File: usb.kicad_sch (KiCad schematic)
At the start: 130 parts, among them J3 USB4105-GF-A, J4 WE_632723300011_alt_symbol, U10 TUSB1046-DCI, U11 TPD4E05U06QDQARQ1, U12 AP22615, U13 TPD4E05U06QDQARQ1, U14 TPD4E05U06QDQARQ1, U15 TPD4E05U06QDQARQ1, U16 TPD4E05U06QDQARQ1, U5 FT230XQ-R, U6 TPS65988, U7 W25Q80DVUXIE_TR, U8 NCP730BMT330TBG, U9 AP22615

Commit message: Renaming Sheets
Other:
- company: Antmicro Ltd -> Dronolab
- title: Jetson Orin Baseboard -> USB Debug, DP
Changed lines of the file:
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@@
   (paper "A3")
   (title_block
-    (title "Jetson Orin Baseboard")
-    (date "2023-03-03")
-    (rev "1.1.0")
-    (company "Antmicro Ltd")
-    (comment 1 "www.antmicro.com")
+    (title "USB Debug, DP")
+    (date "2023-07-05")
+    (rev "1.0.0")
+    (company "Dronolab")
+    (comment 1 "dronolab.etsmtl.ca")
   )
   (junction (at 257.81 152.4) (diameter 0) (color 0 0 0 0)

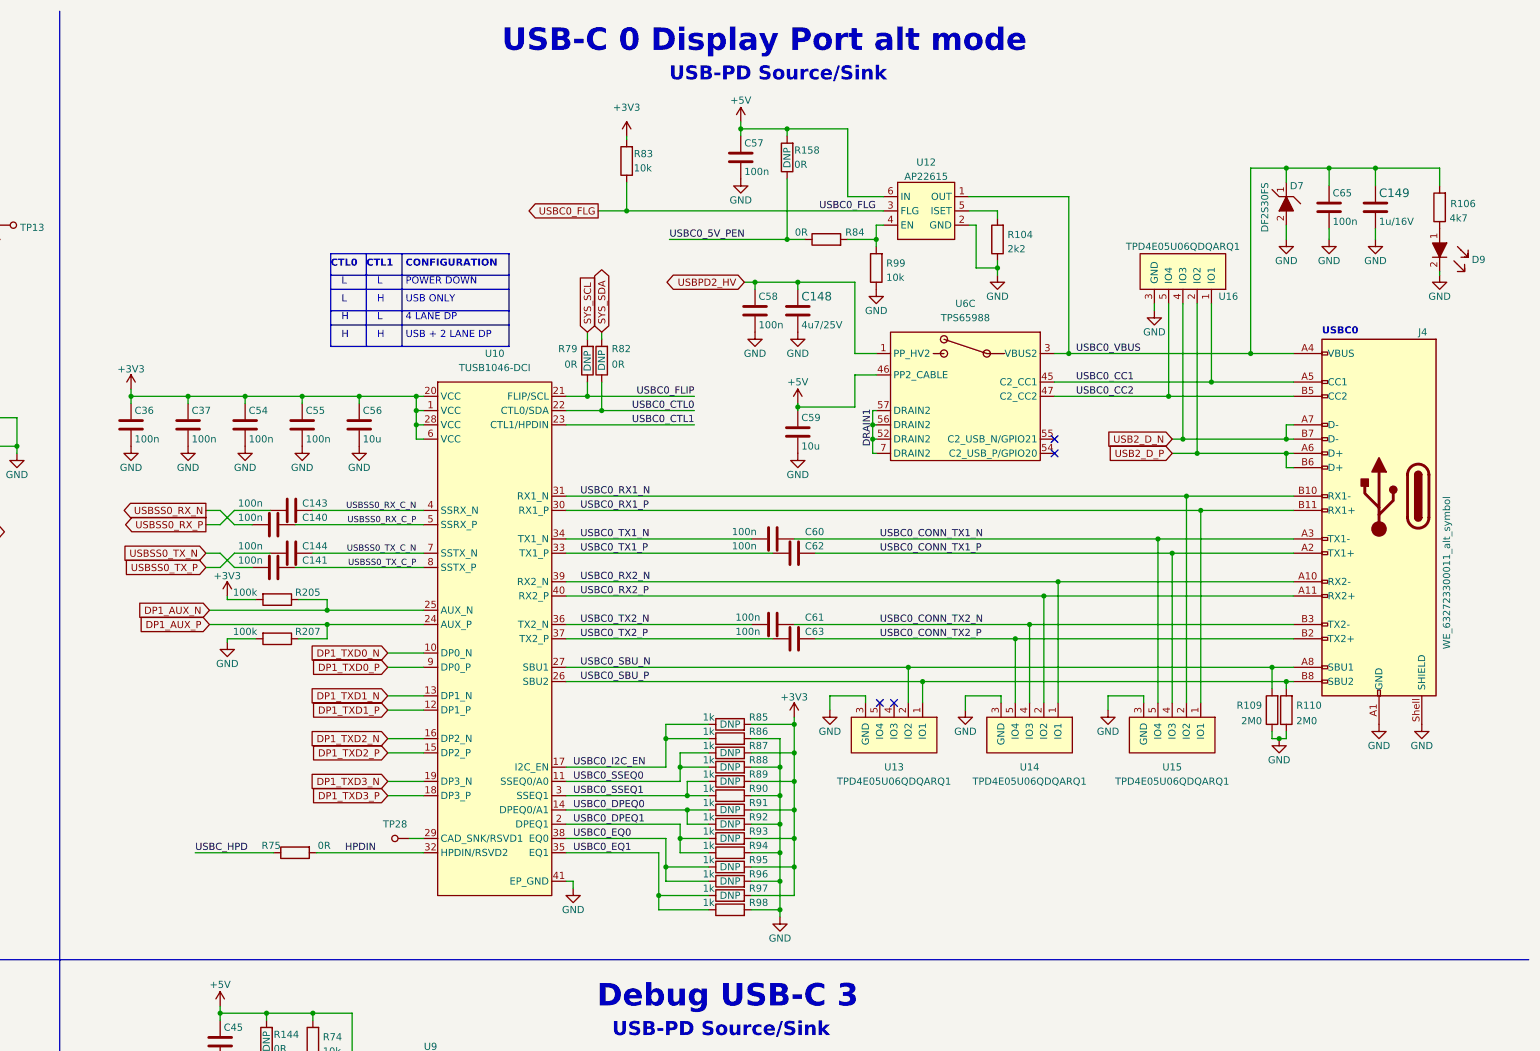
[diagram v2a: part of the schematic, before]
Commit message: Caps and DP to USBC HPD
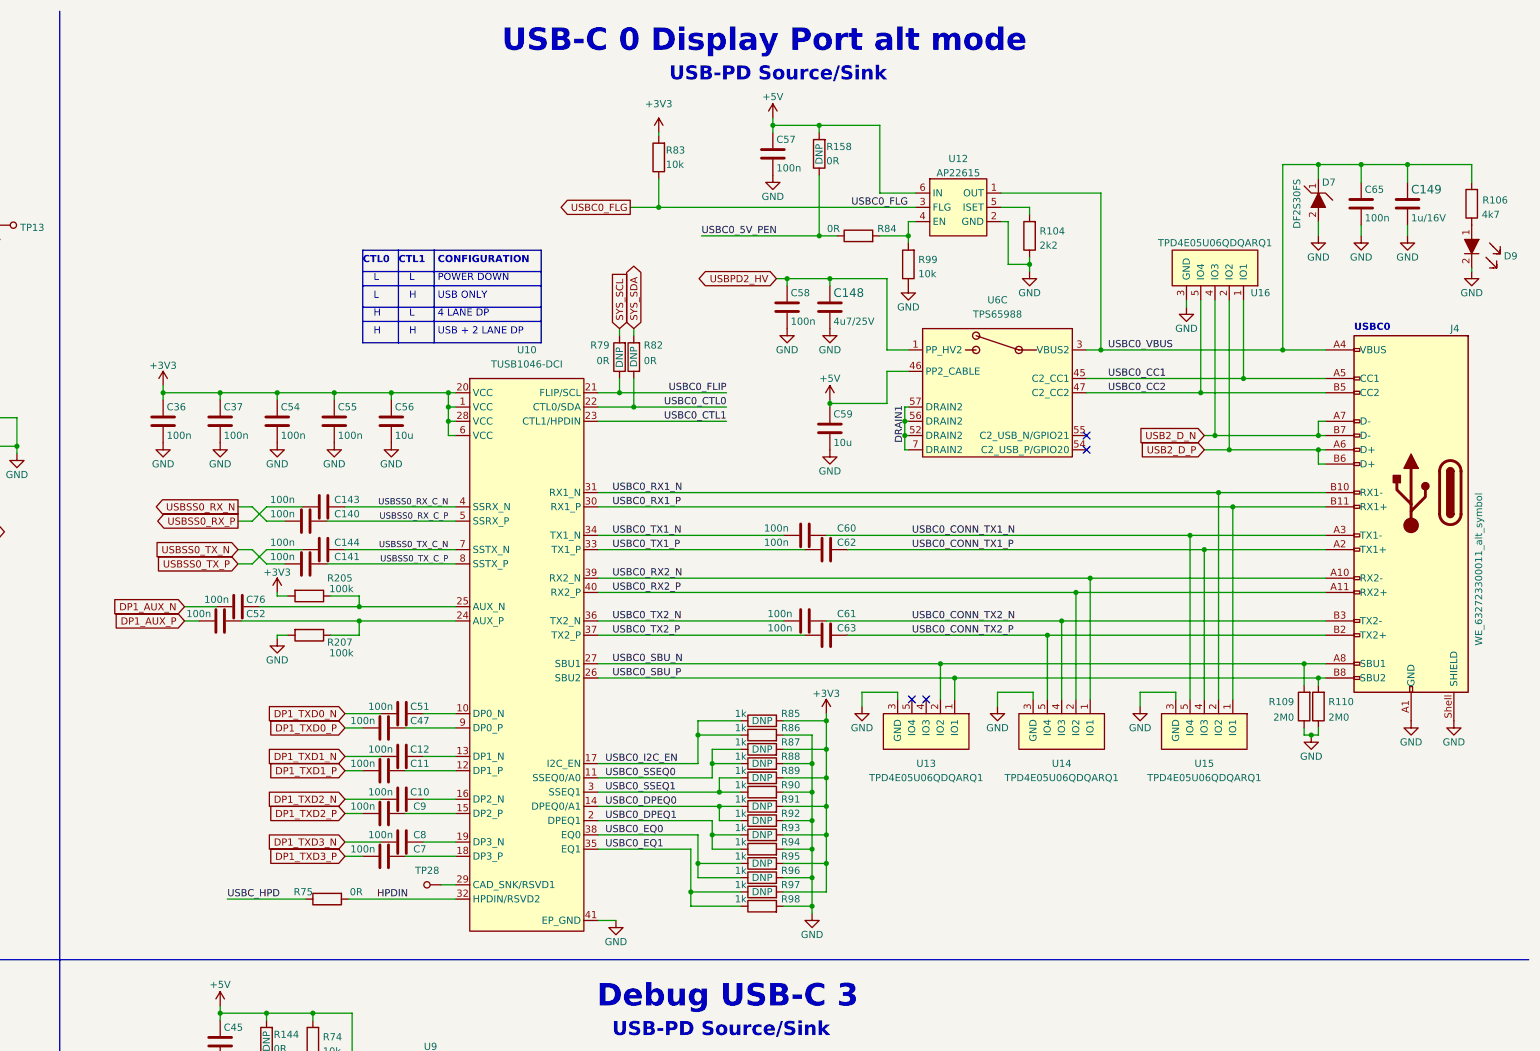
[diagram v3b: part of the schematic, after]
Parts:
- added C10, C11, C12, C47, C51, C52, C7, C76, C8, C9: 100n, symbol Device:C
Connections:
- net DP1_AUX_N: now also C76.1; no longer R205.1, U10.25 (AUX_N)
- net DP1_AUX_P: now also C52.1; no longer R207.1, U10.24 (AUX_P)
- net DP1_TXD0_N: now also C51.1; no longer U10.10 (DP0_N)
- net DP1_TXD0_P: now also C47.1; no longer U10.9 (DP0_P)
- net DP1_TXD1_N: now also C12.1; no longer U10.13 (DP1_N)
- net DP1_TXD1_P: now also C11.1; no longer U10.12 (DP1_P)
- net DP1_TXD2_N: now also C10.1; no longer U10.16 (DP2_N)
- net DP1_TXD2_P: now also C9.1; no longer U10.15 (DP2_P)
- net DP1_TXD3_N: now also C8.1; no longer U10.19 (DP3_N)
- net DP1_TXD3_P: now also C7.1; no longer U10.18 (DP3_P)
- new net: C47.2, U10.9 (DP0_P)
- new net: C76.2, R205.1, U10.25 (AUX_N)
- new net: C52.2, R207.1, U10.24 (AUX_P)
- new net: C11.2, U10.12 (DP1_P)
- new net: C7.2, U10.18 (DP3_P)
- new net: C51.2, U10.10 (DP0_N)
- new net: C12.2, U10.13 (DP1_N)
- new net: C9.2, U10.15 (DP2_P)
- new net: C10.2, U10.16 (DP2_N)
- new net: C8.2, U10.19 (DP3_N)
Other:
- moved on the sheet: C140, C141, C143, C144, C148, C149, C36, C37, C54, C55, C56, C57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

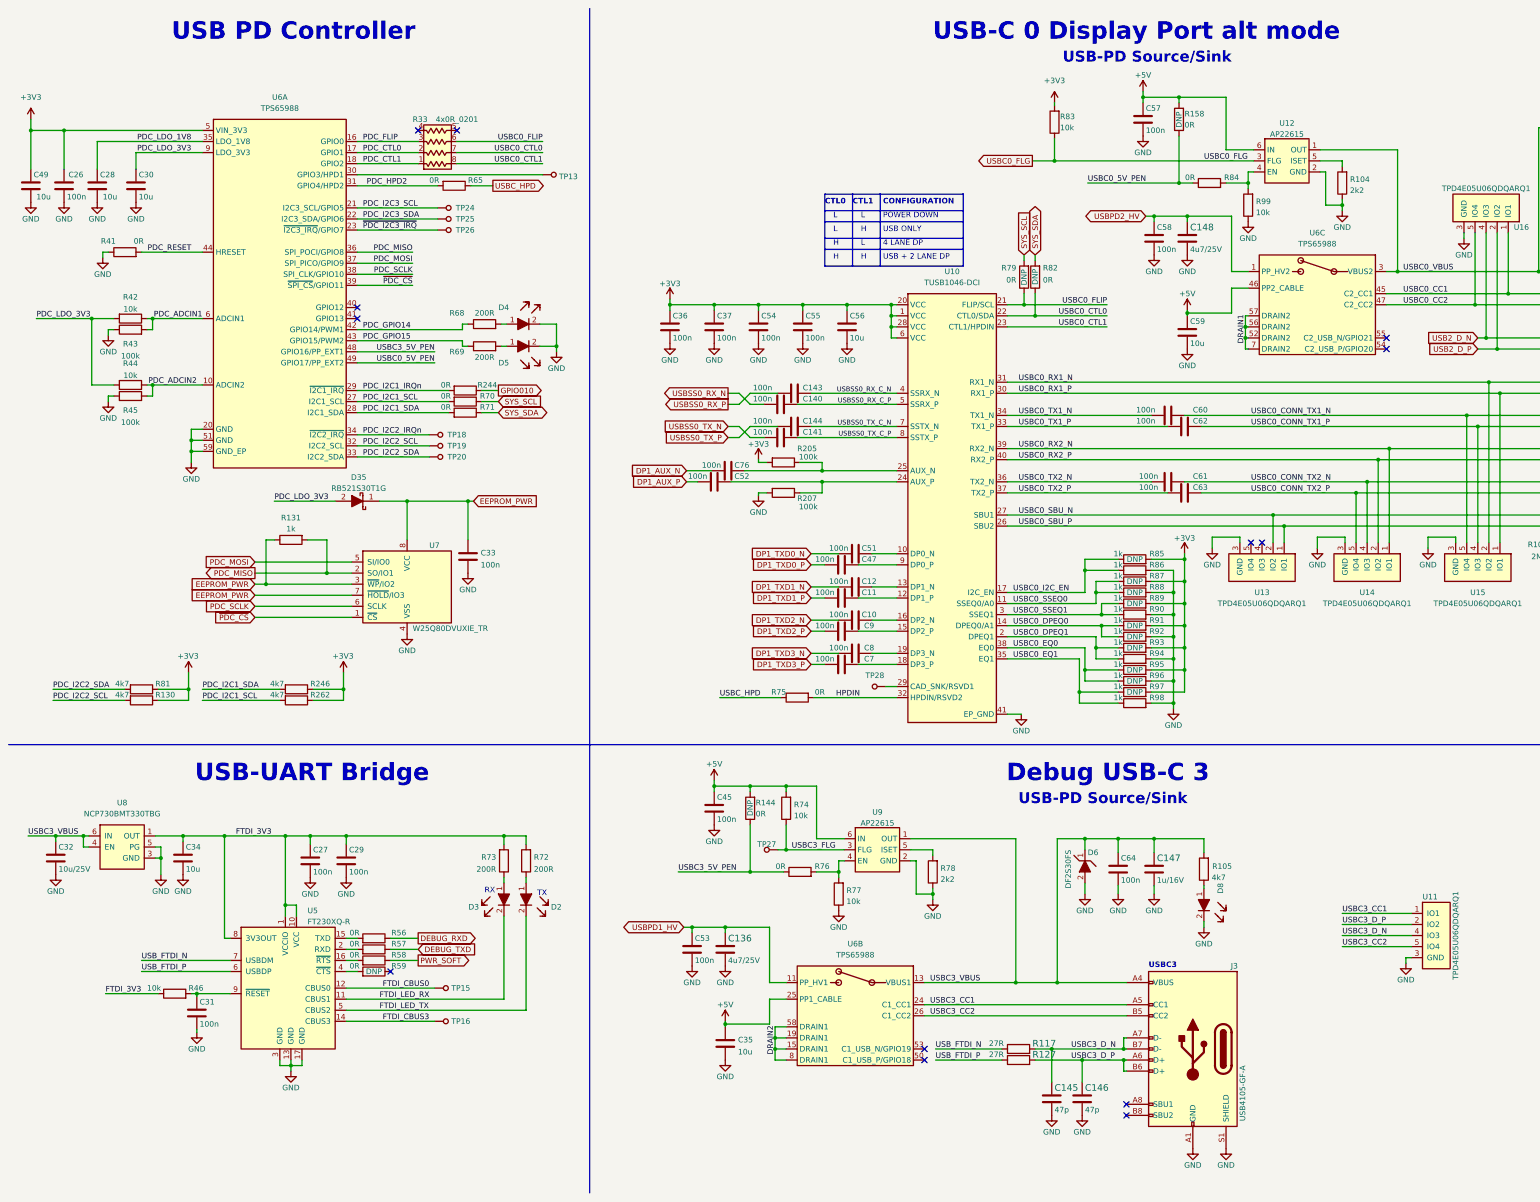
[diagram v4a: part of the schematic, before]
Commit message: Merge du usb-c debug et usb-c 1 et suppression de usb-c 3
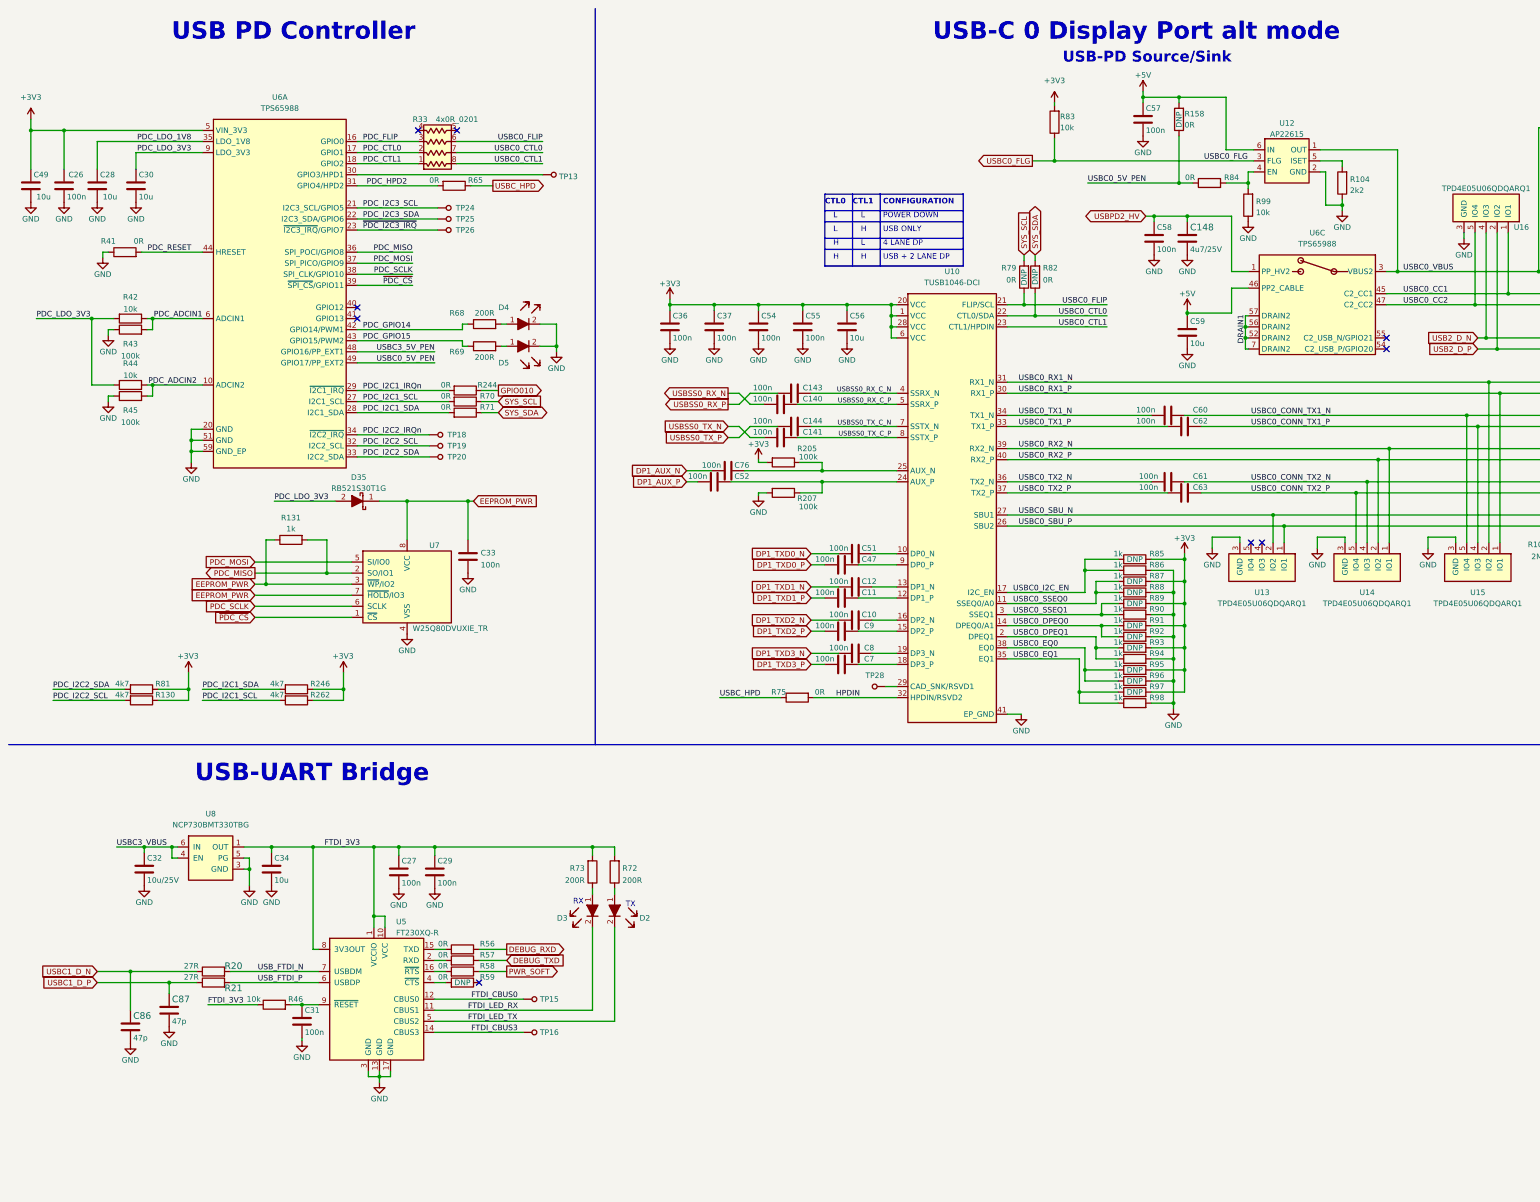
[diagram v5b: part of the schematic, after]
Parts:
- removed C136: C_4u7_0402_25V, jetson-orin-baseboard-footprints:0402-cap, symbol jetson-orin-baseboard:C_4u7_0402_25V
- removed C145, C146: C_47p_0402, jetson-orin-baseboard-footprints:0402-cap, symbol jetson-orin-baseboard:C_47p_0402
- removed C147: C_1u_0402_16V, jetson-orin-baseboard-footprints:0402-cap, symbol jetson-orin-baseboard:C_1u_0402_16V
- removed C35: C_10u_0402, jetson-orin-baseboard-footprints:0402-cap, symbol jetson-orin-baseboard:C_10u_0402
- removed C45, C53, C64: C_100n_0402, jetson-orin-baseboard-footprints:0402-cap, symbol jetson-orin-baseboard:C_100n_0402
- removed D6: DF2S30FS, jetson-orin-baseboard-footprints:SOD-923, symbol jetson-orin-baseboard:DF2S30FS
- removed D8: LTST-C190GKT, jetson-orin-baseboard-footprints:LED_0603, symbol jetson-orin-baseboard:LTST-C190GKT
- removed J3: USB4105-GF-A, jetson-orin-baseboard-footprints:GCT_USB4105-GF-A, symbol jetson-orin-baseboard:USB4105-GF-A
- removed R105: R_4k7_0402, jetson-orin-baseboard-footprints:0402-res, symbol jetson-orin-baseboard:R_4k7_0402
- removed R117, R127: R_27R_0402, jetson-orin-baseboard-footprints:0402-res, symbol jetson-orin-baseboard:R_27R_0402
- removed R144, R76: R_0R_0402, jetson-orin-baseboard-footprints:0402-res, symbol jetson-orin-baseboard:R_0R_0402
- removed R74, R77: R_10k_0402, jetson-orin-baseboard-footprints:0402-res, symbol jetson-orin-baseboard:R_10k_0402
- removed R78: R_2k2_0402, jetson-orin-baseboard-footprints:0402-res, symbol jetson-orin-baseboard:R_2k2_0402
- removed TP27: TP_SMD_0_75MM, jetson-orin-baseboard-footprints:Testpoint_smd_0_75mm, symbol jetson-orin-baseboard:TP_SMD_0_75MM
- removed U11: TPD4E05U06QDQARQ1, jetson-orin-baseboard-footprints:USON-10_2.5x1.0mm_P0.5mm, symbol jetson-orin-baseboard:TPD4E05U06QDQARQ1
- removed unit 2 of U6
- removed U9: AP22615, jetson-orin-baseboard-footprints:TSOT23-6, symbol jetson-orin-baseboard:AP22615
- added C86, C87: C_47p_0402, jetson-orin-baseboard-footprints:0402-cap, symbol jetson-orin-baseboard:C_47p_0402
- added R20, R21: R_27R_0402, jetson-orin-baseboard-footprints:0402-res, symbol jetson-orin-baseboard:R_27R_0402
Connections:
- net GND: now also C86.2, C87.2
- net USB_FTDI_N: now also R20.2
- net USB_FTDI_P: now also R21.2
- new net USBC1_D_N: C86.1, R20.1
- new net USBC1_D_P: C87.1, R21.1
- no-connect marks 13 -> 9
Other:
- note removed: "Debug USB-C 3"
- note removed: "USBC3"
- moved on the sheet: C27, C29, C31, C32, C34, D2, D3, R46, R56, R57, R58, R59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

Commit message: 4G V1 Done
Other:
- moved on the sheet: C27, C29, C31, C32, C34, C86, C87, D2, D3, R20, R21, R46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

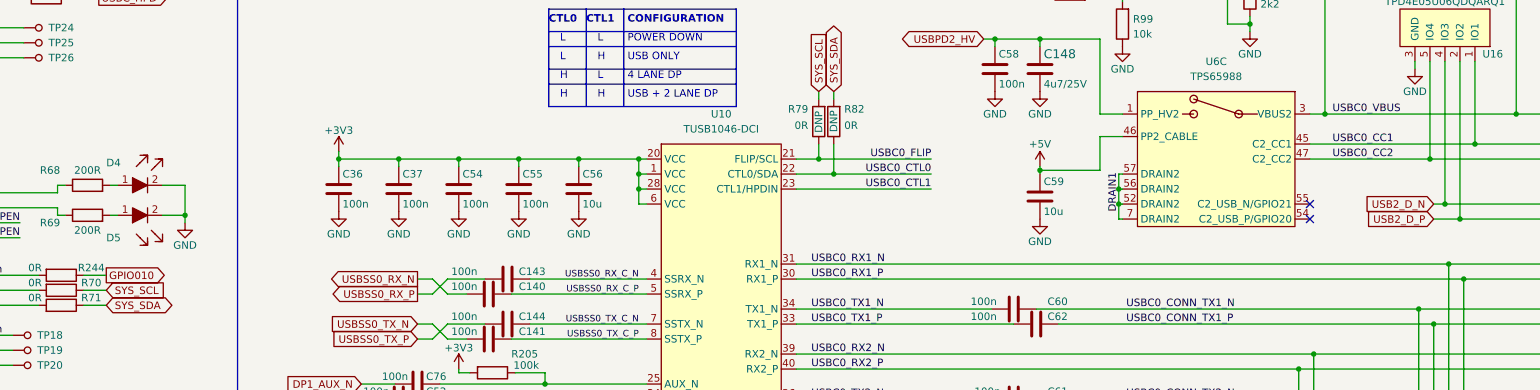
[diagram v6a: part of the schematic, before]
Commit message: Schematic check
Include Pinmux and Schematic Check excels in doc folder and doing a lot of checking and correcting things.
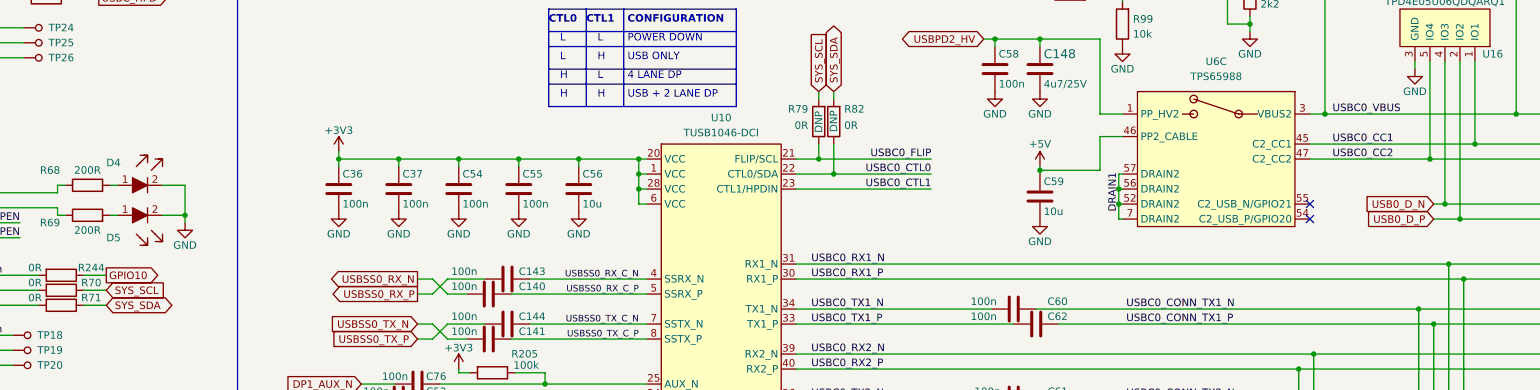
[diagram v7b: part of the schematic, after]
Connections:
- net GPIO010 renamed GPIO10
- net USB2_D_N renamed USB0_D_N
- net USB2_D_P renamed USB0_D_P
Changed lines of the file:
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@@
     )
   )
-  (global_label "USB2_D_P" (shape input) (at 349.885 90.805 180)
+  (global_label "USB0_D_P" (shape input) (at 349.885 90.805 180)
     (effects (font (size 1.27 1.27)) (justify right))
     (property "Intersheetrefs" "${INTERSHEET_REFS}" (at 337.185 90.805 0)
@@
     )
   )
-  (global_label "GPIO010" (shape output) (at 125.095 100.33 0)
+  (global_label "GPIO10" (shape output) (at 125.095 100.33 0)
     (effects (font (size 1.27 1.27)) (justify left))
     (property "Intersheetrefs" "${INTERSHEET_REFS}" (at 135.89 100.33 0)
@@
     )
   )
-  (global_label "USB2_D_N" (shape input) (at 349.885 88.265 180)
+  (global_label "USB0_D_N" (shape input) (at 349.885 88.265 180)
     (effects (font (size 1.27 1.27)) (justify right))
     (property "Intersheetrefs" "${INTERSHEET_REFS}" (at 337.185 88.265 0)
@@
   (symbol (lib_id "jetson-orin-baseboard:TUSB1046-DCI") (at 229.235 118.745 0) (unit 1)
     (in_bom yes) (on_board yes) (dnp no) (fields_autoplaced)
-    (property "Reference" "U10" (at 229.235 73.025 0)
-      (effects (font (size 1.27 1.27)))
-    )
-    (property "Value" "TUSB1046-DCI" (at 229.235 75.565 0)
-      (effects (font (size 1.27 1.27)))
-    )
+    (property "Reference" "U10" (at 229.235 73.66 0)
+      (effects (font (size 1.27 1.27)))
+    )
+    (property "Value" "TUSB1046-DCI" (at 229.235 76.2 0)
+      (effects (font (size 1.27 1.27)))
+    )

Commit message: Small changes
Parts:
- removed C86, C87: C_47p_0402, jetson-orin-baseboard-footprints:0402-cap, symbol jetson-orin-baseboard:C_47p_0402
- removed R20, R21: R_27R_0402, jetson-orin-baseboard-footprints:0402-res, symbol jetson-orin-baseboard:R_27R_0402
